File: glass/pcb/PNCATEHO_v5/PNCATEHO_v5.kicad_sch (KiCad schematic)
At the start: 27 parts, among them J1 TestPoint_2Pole, SW1 SW_PUSH, SW10 SW_PUSH, SW2 SW_PUSH, SW3 SW_PUSH, SW4 SW_PUSH, SW5 SW_PUSH, SW6 SW_PUSH, SW7 SW_PUSH, SW8 SW_PUSH, SW9 SW_PUSH, U1 ProMicro_r

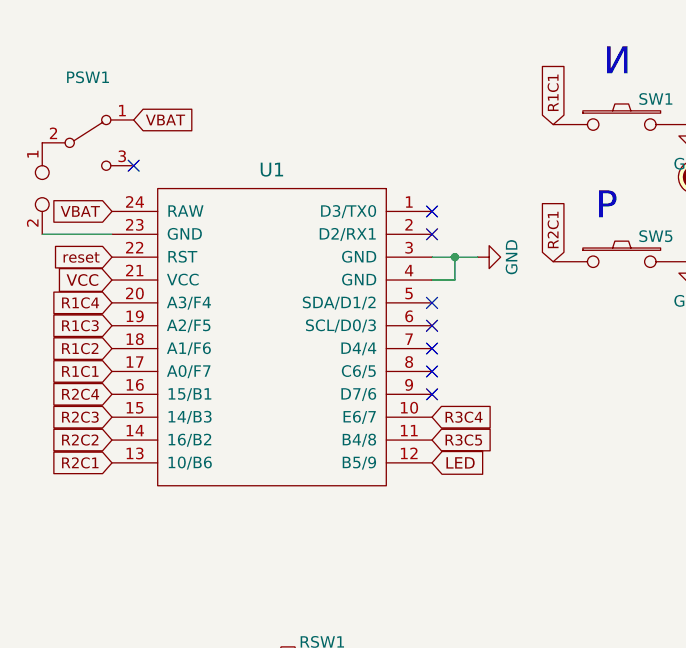
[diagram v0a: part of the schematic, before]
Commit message: Change led pin to TX0
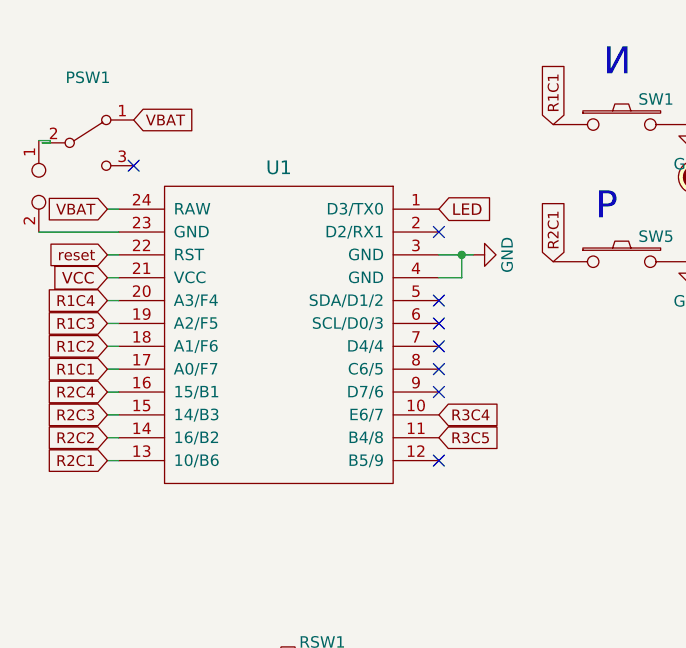
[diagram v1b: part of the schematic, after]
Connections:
- net LED: now also U1.1 (D3/TX0); no longer U1.12 (B5/9)
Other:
- moved on the sheet: U1
